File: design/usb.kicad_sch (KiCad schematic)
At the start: 27 parts, among them J4 USB_B_Mini, SW1 RST, U7 USBLC6-2SC6, U8 SN74LVC1G11DCKR, U9 FT231XS

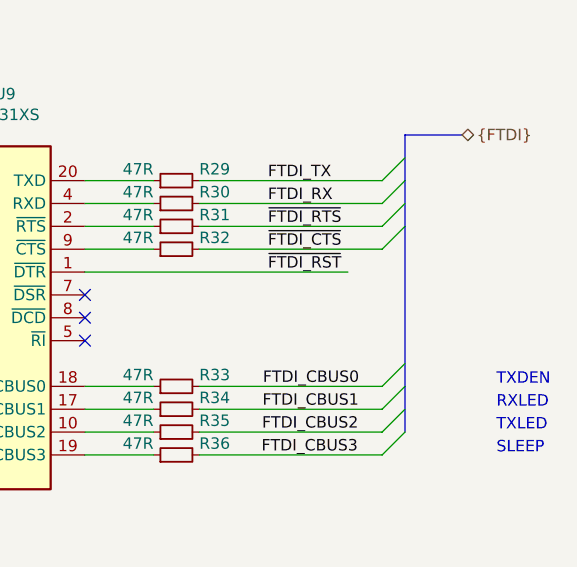
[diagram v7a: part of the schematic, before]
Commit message: Fixed ADC PWRDN problem
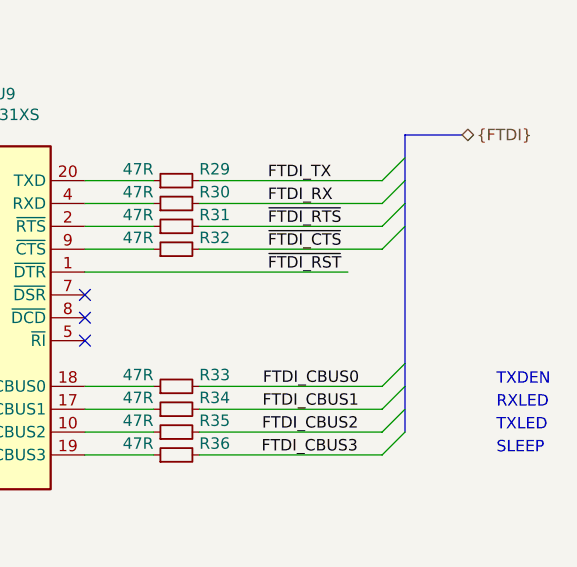
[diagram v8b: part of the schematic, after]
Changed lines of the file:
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@@
-(kicad_sch (version 20200608) (host eeschema "5.99.0-unknown-ad69e44~101~ubuntu18.04.1")
-  (page 4 8)
+(kicad_sch (version 20200618) (host eeschema "5.99.0-unknown-f420396~101~ubuntu18.04.1")
+  (page 1 8)
   (paper "A4")
   (title_block
@@
   )
   (bus_alias "FTDI" (members "FTDI_TX" "FTDI_RX" "~FTDI_RTS" "~FTDI_CTS" "FTDI_CBUS[0..3]"))
-  (junction (at 20.32 26.67))
-  (junction (at 39.37 118.11))
-  (junction (at 57.15 153.67))
-  (junction (at 67.31 153.67))
-  (junction (at 69.85 101.6))
-  (junction (at 96.52 156.21))
-  (junction (at 119.38 151.13))
-  (junction (at 128.27 85.09))
-  (junction (at 140.97 87.63))
-  (junction (at 187.96 68.58))
-  (junction (at 190.5 68.58))
-  (junction (at 190.5 116.84))
+  (junction (at 20.32 26.67) (diameter 0) (color 0 0 0 0))
+  (junction (at 39.37 118.11) (diameter 0) (color 0 0 0 0))
+  (junction (at 57.15 153.67) (diameter 0) (color 0 0 0 0))
+  (junction (at 67.31 153.67) (diameter 0) (color 0 0 0 0))
+  (junction (at 69.85 101.6) (diameter 0) (color 0 0 0 0))
+  (junction (at 96.52 156.21) (diameter 0) (color 0 0 0 0))
+  (junction (at 119.38 151.13) (diameter 0) (color 0 0 0 0))
+  (junction (at 128.27 85.09) (diameter 0) (color 0 0 0 0))
+  (junction (at 140.97 87.63) (diameter 0) (color 0 0 0 0))
+  (junction (at 187.96 68.58) (diameter 0) (color 0 0 0 0))
+  (junction (at 190.5 68.58) (diameter 0) (color 0 0 0 0))
+  (junction (at 190.5 116.84) (diameter 0) (color 0 0 0 0))
   (no_connect (at 46.99 111.76))
-  (no_connect (at 172.72 77.47))
   (no_connect (at 208.28 95.25))
   (no_connect (at 208.28 90.17))
+  (no_connect (at 172.72 77.47))
   (no_connect (at 208.28 92.71))
-  (bus_entry (at 241.3 77.47) (size 2.54 -2.54))
-  (bus_entry (at 241.3 80.01) (size 2.54 -2.54))
-  (bus_entry (at 241.3 82.55) (size 2.54 -2.54))
-  (bus_entry (at 241.3 85.09) (size 2.54 -2.54))
-  (bus_entry (at 241.3 100.33) (size 2.54 -2.54))
-  (bus_entry (at 241.3 102.87) (size 2.54 -2.54))
-  (bus_entry (at 241.3 105.41) (size 2.54 -2.54))
-  (bus_entry (at 241.3 107.95) (size 2.54 -2.54))
+  (bus_entry (at 241.3 77.47) (size 2.54 -2.54)
+    (stroke (width 0.1524) (type solid) (color 0 0 0 0))
+  )
+  (bus_entry (at 241.3 80.01) (size 2.54 -2.54)
+    (stroke (width 0.1524) (type solid) (color 0 0 0 0))
+  )
+  (bus_entry (at 241.3 82.55) (size 2.54 -2.54)
+    (stroke (width 0.1524) (type solid) (color 0 0 0 0))
+  )
+  (bus_entry (at 241.3 85.09) (size 2.54 -2.54)
+    (stroke (width 0.1524) (type solid) (color 0 0 0 0))
+  )
+  (bus_entry (at 241.3 100.33) (size 2.54 -2.54)
+    (stroke (width 0.1524) (type solid) (color 0 0 0 0))
+  )
+  (bus_entry (at 241.3 102.87) (size 2.54 -2.54)
+    (stroke (width 0.1524) (type solid) (color 0 0 0 0))
+  )
+  (bus_entry (at 241.3 105.41) (size 2.54 -2.54)
+    (stroke (width 0.1524) (type solid) (color 0 0 0 0))
+  )
+  (bus_entry (at 241.3 107.95) (size 2.54 -2.54)
+    (stroke (width 0.1524) (type solid) (color 0 0 0 0))
+  )
   (wire (pts (xy 20.32 25.4) (xy 20.32 26.67))
     (stroke (width 0) (type solid) (color 0 0 0 0))
@@
     (stroke (width 0) (type solid) (color 0 0 0 0))
   )
-  (bus (pts (xy 243.84 77.47) (xy 243.84 82.55))
-    (stroke (width 0) (type solid) (color 0 0 0 0))
-  )
-  (bus (pts (xy 243.84 82.55) (xy 243.84 100.33))
-    (stroke (width 0) (type solid) (color 0 0 0 0))
-  )
+  (bus (pts (xy 243.84 77.47) (xy 243.84 80.01))
+    (stroke (width 0) (type solid) (color 0 0 0 0))
+  )
+  (bus (pts (xy 243.84 80.01) (xy 243.84 97.79))
+    (stroke (width 0) (type solid) (color 0 0 0 0))
+  )
+  (bus (pts (xy 243.84 97.79) (xy 243.84 100.33))
+    (stroke (width 0) (type solid) (color 0 0 0 0))
+  )
